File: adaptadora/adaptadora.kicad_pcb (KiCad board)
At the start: 2 copper layers, 200 x 100 mm, 107 parts, among them J1 Conn_Coaxial, J10 Conn_Coaxial, J11 Conn_Coaxial, J12 Conn_Coaxial, J13 Conn_Coaxial, J14 Conn_Coaxial, J15 Conn_Coaxial, J16 Conn_Coaxial, J17 Conn_Coaxial, J18 Conn_Coaxial, J19 Conn_Coaxial, J2 Conn_Coaxial, J20 Conn_Coaxial, J22 Conn_Coaxial, J3 Conn_Coaxial, J4 Conn_Coaxial, J5 Conn_02x20_Odd_Even, J6 Conn_01x02, J7 Conn_02x20_Odd_Even, J8 Conn_01x04, J9 Conn_01x02, U11 LM361MX_NOPB, U12 LM361MX_NOPB, U13 LM361MX_NOPB, U14 LM361MX_NOPB, U21 TLV2772IDR, U22 TLV2772IDR, U23 TLV2772IDR, U25 TLV2772IDR, U31 SN74LVC2T45DCUR, U32 SN74LVC2T45DCUR

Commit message: se ordenan campos de integrados
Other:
- board text added: "Grilla para diseño del PCB: 50 mils Grilla para el trazado de bordes de PCB: 39,37 mils (1 mm)"
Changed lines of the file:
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@@
   (general
     (thickness 1.6)
-    (drawings 31)
+    (drawings 32)
     (tracks 0)
     (zones 0)
@@
     (46 B.CrtYd user)
     (47 F.CrtYd user)
-    (48 B.Fab user hide)
-    (49 F.Fab user hide)
+    (48 B.Fab user)
+    (49 F.Fab user)
   )
   (setup
@@
     )
   )
+  (gr_text "Grilla para diseño del PCB: 50 mils\nGrilla para el trazado de bordes de PCB: 39,37 mils (1 mm)" (at 101 157) (layer Cmts.User)
+    (effects (font (size 1 1) (thickness 0.15)))
+  )
   (gr_text +3.3V (at 48.26 97.79) (layer F.SilkS)

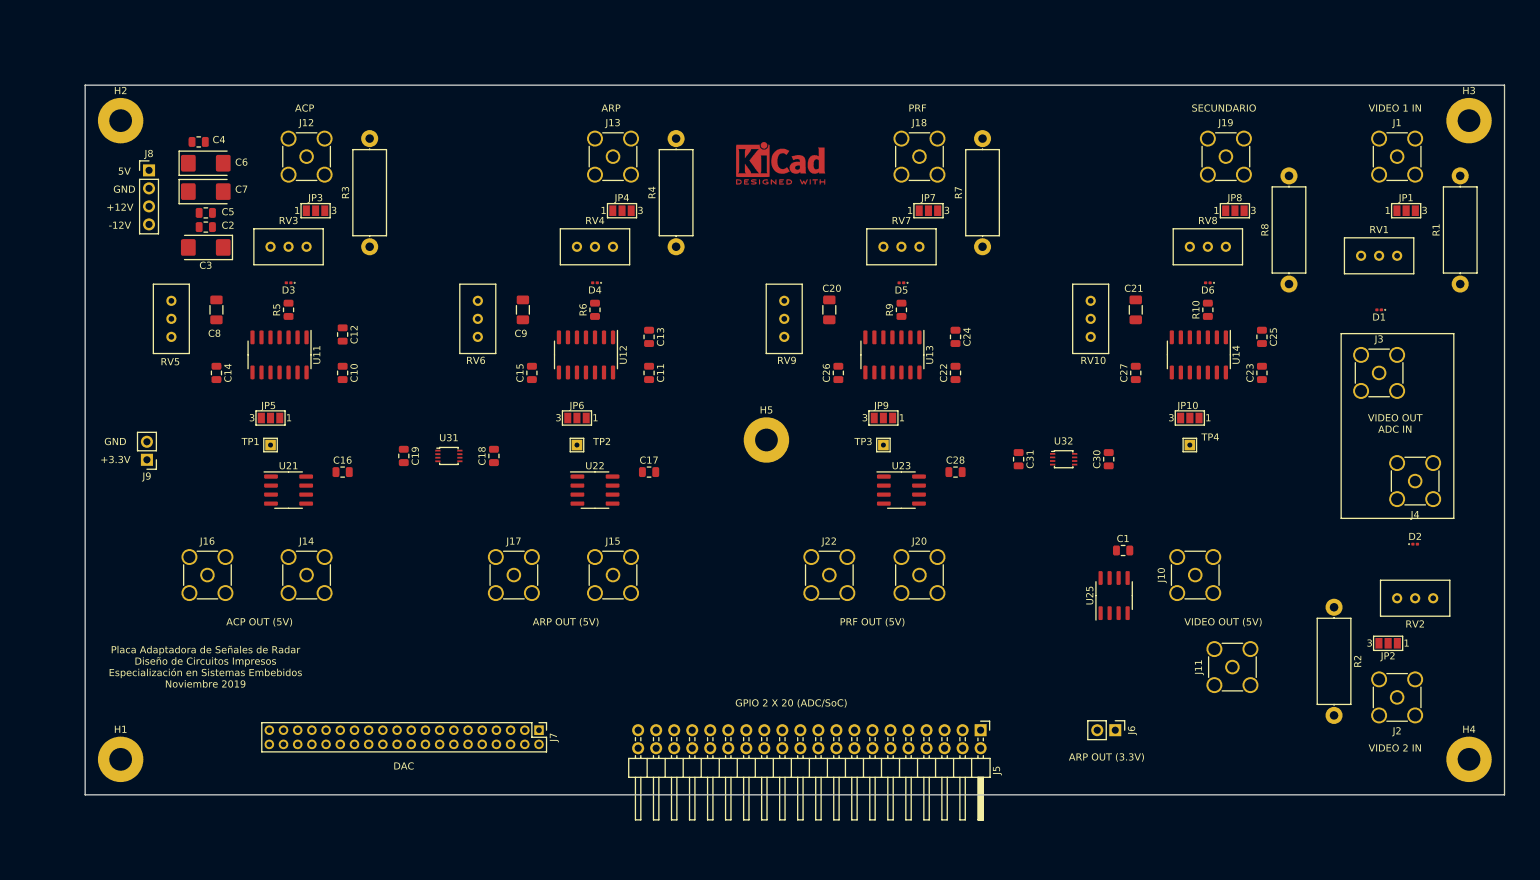
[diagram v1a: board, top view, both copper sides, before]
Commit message: se cambia footprint de componentes y el posicionamiento
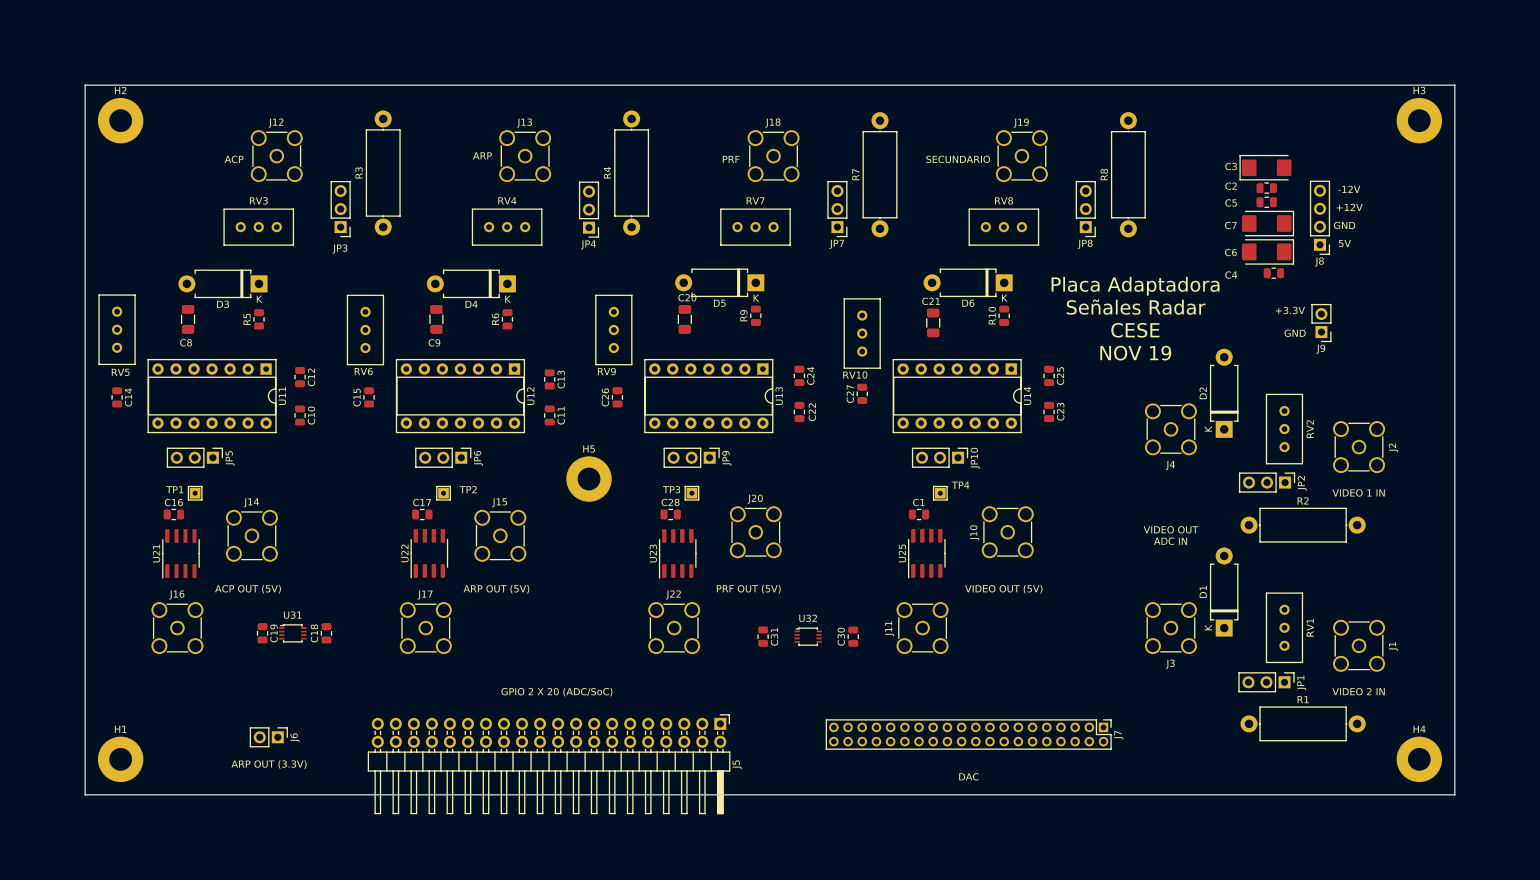
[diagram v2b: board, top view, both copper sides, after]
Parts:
- removed REF**: KiCad-Logo2_5mm_Copper, Symbol:KiCad-Logo2_5mm_Copper
- C1, C10, C11, C12, C13, C14, C15, C16, C17, C18, C19, C2, C22, C23, C24, C25, C26, C27, C28, C30, C31, C4, C5: value 0.1uF-50V -> 0_1uF-50V
- C3, C6, C7: value 2.2uF-35V -> 2_2uF-35V
- D1, D2, D3, D4, D5, D6: footprint Diode_SMD:D_0201_0603Metric -> Diode_THT:D_DO-15_P10.16mm_Horizontal
- JP1, JP10, JP2, JP3, JP4, JP5, JP6, JP7, JP8, JP9: footprint Jumper:SolderJumper-3_P1.3mm_Open_Pad1.0x1.5mm_NumberLabels -> Connector_PinHeader_2.54mm:PinHeader_1x03_P2.54mm_Vertical
- U11, U12, U13, U14: footprint Package_SO:SOIC-14_3.9x8.7mm_P1.27mm -> Package_DIP:DIP-14_W7.62mm_Socket
- moved J9 166.5 mm to (218.2, 79.8)
- moved J8 165.3 mm to (218.0, 67.5), turned to 180 degrees
- moved C4 152.6 mm to (211.5, 71.5), turned to 180 degrees
- moved C6 150.0 mm to (210.5, 68.5), turned to 180 degrees
- moved C3 149.9 mm to (210.5, 56.6), turned to 0 degrees
- moved C2 149.6 mm to (210.5, 59.5)
- moved C7 149.6 mm to (210.5, 64.5), turned to 180 degrees
- moved C5 149.5 mm to (210.5, 61.5), turned to 180 degrees
- moved J6 118.0 mm to (71.2, 136.9)
- moved J7 79.6 mm to (187.5, 135.5)
- moved J1 69.1 mm to (223.5, 124.0), turned to 270 degrees
- moved R1 68.7 mm to (208.0, 135.0), turned to 0 degrees
- moved JP1 68.6 mm to (213.0, 129.1), turned to 270 degrees
- moved RV1 57.2 mm to (213.0, 124.0), turned to 270 degrees
- moved D1 49.9 mm to (204.5, 121.5), turned to 90 degrees
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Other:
- board size 200 x 100 mm -> 193 x 100 mm
- board text added: "Grilla para diseño del PCB: 39,37 mils (1 mm) Grilla para el trazado de bordes de PCB: 39,37 mils (1 mm)"
- board text added: "Placa Adaptadora Señales Radar CESE NOV 19"
- board text removed: "Grilla para diseño del PCB: 50 mils Grilla para el trazado de bordes de PCB: 39,37 mils (1 mm)"
- board text removed: "Placa Adaptadora de Señales de Radar Diseño de Circuitos Impresos Especialización en Sistemas Embebidos Noviembre 2019"

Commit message: agrego modelo 3d lm361 sobre el sócalo
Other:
- board text added: "DCI-CESE Diseño Argentino"
- board text added: "Placa Adaptadora Señales Radar Rev. 0 - Nov 19"
- board text removed: "Placa Adaptadora Señales Radar CESE NOV 19"
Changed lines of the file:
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@@
   (general
     (thickness 1.6)
-    (drawings 28)
+    (drawings 29)
     (tracks 0)
     (zones 0)
@@
   )
   (layers
-    (0 F.Cu signal hide)
-    (31 B.Cu signal hide)
-    (32 B.Adhes user hide)
-    (33 F.Adhes user hide)
-    (34 B.Paste user hide)
-    (35 F.Paste user hide)
-    (36 B.SilkS user hide)
-    (37 F.SilkS user hide)
-    (38 B.Mask user hide)
-    (39 F.Mask user hide)
-    (40 Dwgs.User user hide)
-    (41 Cmts.User user hide)
-    (42 Eco1.User user hide)
-    (43 Eco2.User user hide)
-    (44 Edge.Cuts user hide)
-    (45 Margin user hide)
-    (46 B.CrtYd user hide)
-    (47 F.CrtYd user hide)
-    (48 B.Fab user hide)
-    (49 F.Fab user hide)
+    (0 F.Cu signal)
+    (31 B.Cu signal)
+    (32 B.Adhes user)
+    (33 F.Adhes user)
+    (34 B.Paste user)
+    (35 F.Paste user)
+    (36 B.SilkS user)
+    (37 F.SilkS user)
+    (38 B.Mask user)
+    (39 F.Mask user)
+    (40 Dwgs.User user)
+    (41 Cmts.User user)
+    (42 Eco1.User user)
+    (43 Eco2.User user)
+    (44 Edge.Cuts user)
+    (45 Margin user)
+    (46 B.CrtYd user)
+    (47 F.CrtYd user)
+    (48 B.Fab user)
+    (49 F.Fab user)
   )
   (setup
@@
       (rotate (xyz 0 0 0))
     )
+    (model ${KISYS3DMOD}/Package_DIP.3dshapes/DIP-14_W7.62mm.wrl
+      (offset (xyz 0 0 4))
+      (scale (xyz 1 1 1))
+      (rotate (xyz 0 0 0))
+    )
   )
   (module Package_DIP:DIP-14_W7.62mm_Socket (layer F.Cu)
@@
       (rotate (xyz 0 0 0))
     )
+    (model ${KISYS3DMOD}/Package_DIP.3dshapes/DIP-14_W7.62mm.wrl
+      (offset (xyz 0 0 4))
+      (scale (xyz 1 1 1))
+      (rotate (xyz 0 0 0))
+    )
   )
   (module Package_DIP:DIP-14_W7.62mm_Socket (layer F.Cu)
@@
       (rotate (xyz 0 0 0))
     )
+    (model ${KISYS3DMOD}/Package_DIP.3dshapes/DIP-14_W7.62mm.wrl
+      (offset (xyz 0 0 4))
+      (scale (xyz 1 1 1))
+      (rotate (xyz 0 0 0))
+    )
   )
   (module Package_DIP:DIP-14_W7.62mm_Socket (layer F.Cu)
@@
       (rotate (xyz 0 0 0))
     )
+    (model ${KISYS3DMOD}/Package_DIP.3dshapes/DIP-14_W7.62mm.wrl
+      (offset (xyz 0 0 4))
+      (scale (xyz 1 1 1))
+      (rotate (xyz 0 0 0))
+    )
   )
   (module Diode_THT:D_DO-15_P10.16mm_Horizontal (layer F.Cu)
@@
     (descr "Through hole straight pin header, 1x04, 2.54mm pitch, single row")
     (tags "Through hole pin header THT 1x04 2.54mm single row")
-    (fp_text reference J8 (at 0 -2.33) (layer F.SilkS)
+    (fp_text reference J8 (at 0 -3) (layer F.SilkS)
       (effects (font (size 1 1) (thickness 0.15)))
     )
@@
     (descr "Through hole straight pin header, 1x02, 2.54mm pitch, single row")
     (tags "Through hole pin header THT 1x02 2.54mm single row")
-    (fp_text reference J9 (at 0 -2.33) (layer F.SilkS)
+    (fp_text reference J9 (at 0 -2.71) (layer F.SilkS)
       (effects (font (size 1 1) (thickness 0.15)))
     )
@@
     (tags "test point THT pad rectangle square")
     (attr virtual)
-    (fp_text reference TP1 (at -2.81 -0.46) (layer F.SilkS)
+    (fp_text reference TP1 (at 3 -0.5) (layer F.SilkS)
       (effects (font (size 1 1) (thickness 0.15)))
     )
@@
     )
   )
+  (gr_text "DCI-CESE\nDiseño\nArgentino\n" (at 53.5 62) (layer F.SilkS)
+    (effects (font (size 1.5 1.5) (thickness 0.2)))
+  )
   (dimension 193 (width 0.15) (layer Dwgs.User)
     (gr_text "193,000 mm" (at 140.5 34.7) (layer Dwgs.User)
@@
     (effects (font (size 1 1) (thickness 0.15)))
   )
-  (gr_text +3.3V (at 213.76 76.79) (layer F.SilkS)
+  (gr_text +3.3V (at 222.5 76.79) (layer F.SilkS)
     (effects (font (size 1 1) (thickness 0.15)))
   )
-  (gr_text GND (at 214.5 80) (layer F.SilkS)
+  (gr_text GND (at 222 80) (layer F.SilkS)
     (effects (font (size 1 1) (thickness 0.15)))
   )
@@
     (effects (font (size 1 1) (thickness 0.15)))
   )
-  (gr_text "Placa Adaptadora \nSeñales Radar\nCESE\nNOV 19" (at 192 78) (layer F.SilkS)
-    (effects (font (size 2 2) (thickness 0.15)))
+  (gr_text "Placa Adaptadora \nSeñales Radar\nRev. 0 - Nov 19" (at 195 76.5) (layer F.SilkS)
+    (effects (font (size 1.5 1.5) (thickness 0.2)))
   )
   (dimension 100 (width 0.15) (layer Dwgs.User)

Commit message: ruteo en proceso
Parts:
- R10: value 100 - 1/8W - 5% -> 100-1/8W-5%
- moved J7 38.5 mm to (149.0, 137.0), turned to 90 degrees
- moved J20 17.9 mm to (120.8, 110.5)
- moved C19 15.4 mm to (84.0, 125.8), turned to 180 degrees
- moved U31 14.6 mm to (87.8, 124.0), turned to 90 degrees
- moved C16 13.2 mm to (69.8, 105.5)
- moved C17 13.2 mm to (104.8, 105.5)
- moved J16 13.2 mm to (70.2, 121.5)
- moved J17 13.2 mm to (105.2, 121.5)
- moved U21 13.2 mm to (70.8, 111.0)
- moved U22 13.2 mm to (105.8, 111.0)
- moved C14 12.4 mm to (57.0, 80.0)
- moved C15 12.0 mm to (92.0, 80.0), turned to 270 degrees
- moved C26 12.0 mm to (127.0, 80.0), turned to 270 degrees
- moved C27 12.0 mm to (162.0, 80.0), turned to 270 degrees
- moved J14 9.71 mm to (58.0, 110.5)
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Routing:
- net GND: track 0.00 -> 362.7 mm
- net +5V: track 0.00 -> 347.8 mm, vias 0 -> 2
- net -12V: track 0.00 -> 208.2 mm
- net +12V: track 0.00 -> 192.9 mm
- net Net-(C9-Pad1): track 0.00 -> 20.3 mm
- net Net-(C20-Pad1): track 0.00 -> 20.3 mm
- net Net-(C8-Pad1): track 0.00 -> 20.3 mm
- net Net-(J13-Pad1): track 0.00 -> 19.0 mm
- net Net-(J19-Pad1): track 0.00 -> 19.0 mm
- net Net-(J18-Pad1): track 0.00 -> 19.0 mm
- net Net-(J12-Pad1): track 0.00 -> 19.0 mm
- net Net-(C21-Pad1): track 0.00 -> 17.8 mm
- net Net-(D2-Pad1): track 0.00 -> 16.0 mm
- net Net-(D1-Pad1): track 0.00 -> 16.0 mm
- net Net-(J1-Pad1): track 0.00 -> 15.6 mm
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
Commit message: ruteo en proceso
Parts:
- moved J20 24.3 mm to (141.0, 124.0)
- moved J14 18.7 mm to (71.0, 124.0)
- moved J15 17.5 mm to (106.0, 124.0)
- moved J10 16.1 mm to (176.0, 124.0)
- moved C18 15.7 mm to (78.0, 108.0)
- moved C19 15.7 mm to (78.0, 111.2)
- moved U31 15.7 mm to (81.8, 109.5)
- moved C30 13.4 mm to (144.2, 108.0)
- moved C31 13.4 mm to (144.2, 111.0)
- moved U32 13.2 mm to (149.0, 109.6)
- moved J16 11.5 mm to (59.0, 124.0)
- moved J17 11.5 mm to (94.0, 124.0)
- moved U21 11.3 mm to (59.5, 109.5), turned to 0 degrees
- moved U22 11.3 mm to (94.5, 109.5), turned to 0 degrees
- moved C28 9.71 mm to (136.0, 107.5)
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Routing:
- net GND: track 362.7 -> 273.4 mm
- net /Señales de ACP y ARP/ACP: track 5.02 -> 43.3 mm
- net /Señales de ACP y ARP/ARP: track 5.02 -> 33.8 mm
- net Net-(J14-Pad1): track 0.00 -> 19.9 mm
- net Net-(J20-Pad1): track 1.11 -> 20.1 mm
- net Net-(J15-Pad1): track 1.14 -> 20.1 mm
- net /Señales de Video Secundario y PRF/VIDEO_COMP: track 5.02 -> 23.0 mm
- net /Señales de Video Secundario y PRF/PRF: track 5.02 -> 18.6 mm
- net Net-(J10-Pad1): track 13.8 -> 25.9 mm
- net Net-(J22-Pad1): track 9.35 -> 19.7 mm
- net Net-(J17-Pad1): track 9.38 -> 19.7 mm
- net Net-(J16-Pad1): track 9.35 -> 19.3 mm
- net +3V3: track 0.00 -> 5.25 mm
- net Net-(J11-Pad1): track 9.34 -> 13.2 mm
- net +5V: track 347.8 -> 349.2 mm

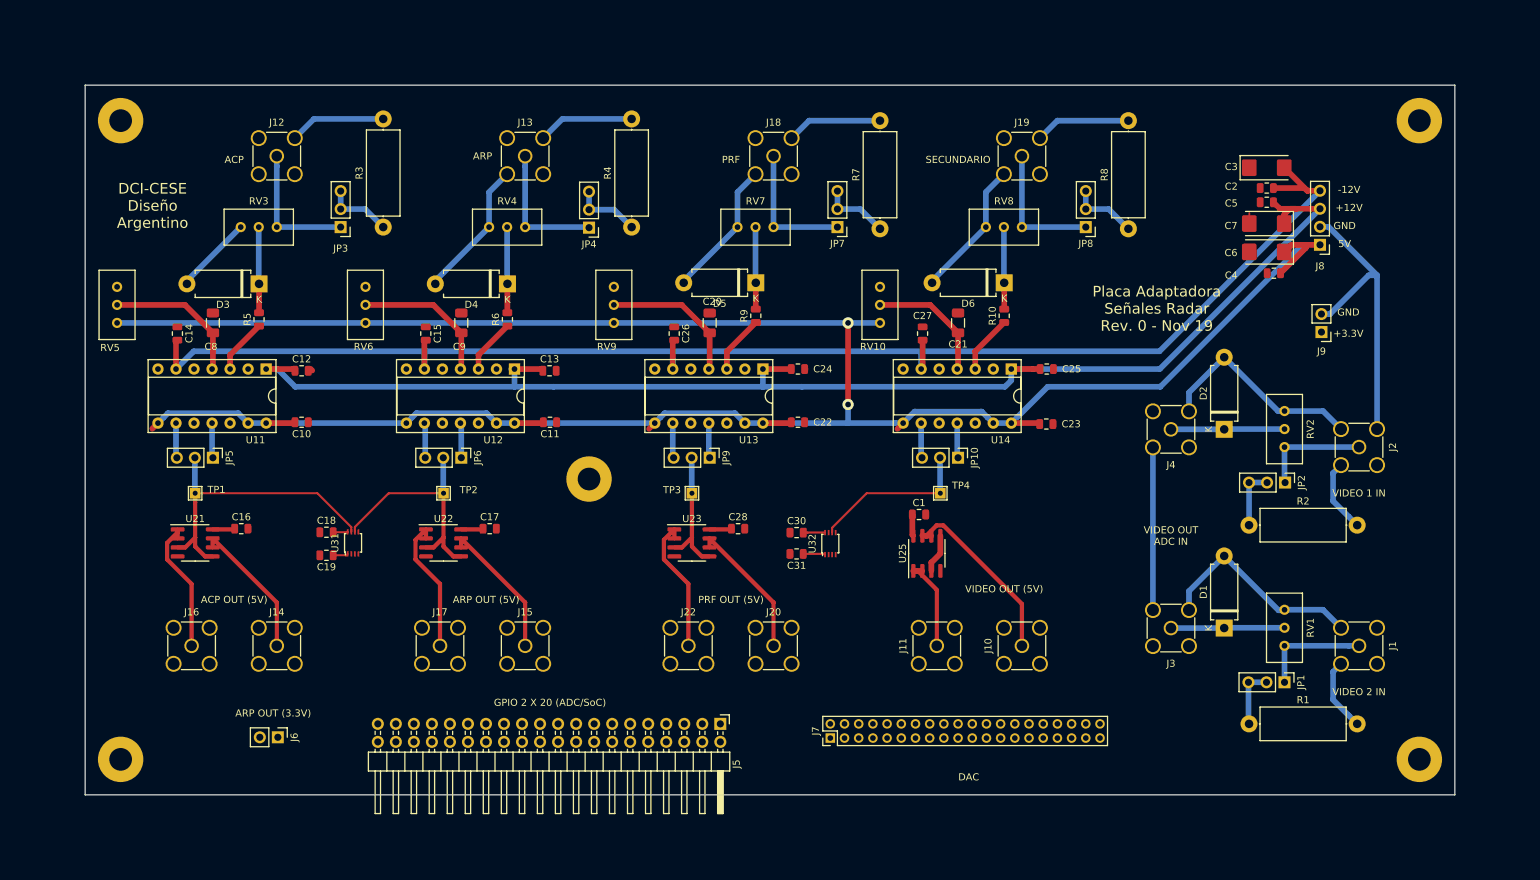
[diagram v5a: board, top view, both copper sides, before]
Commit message: ultimo commit antes de quitar dac del esq
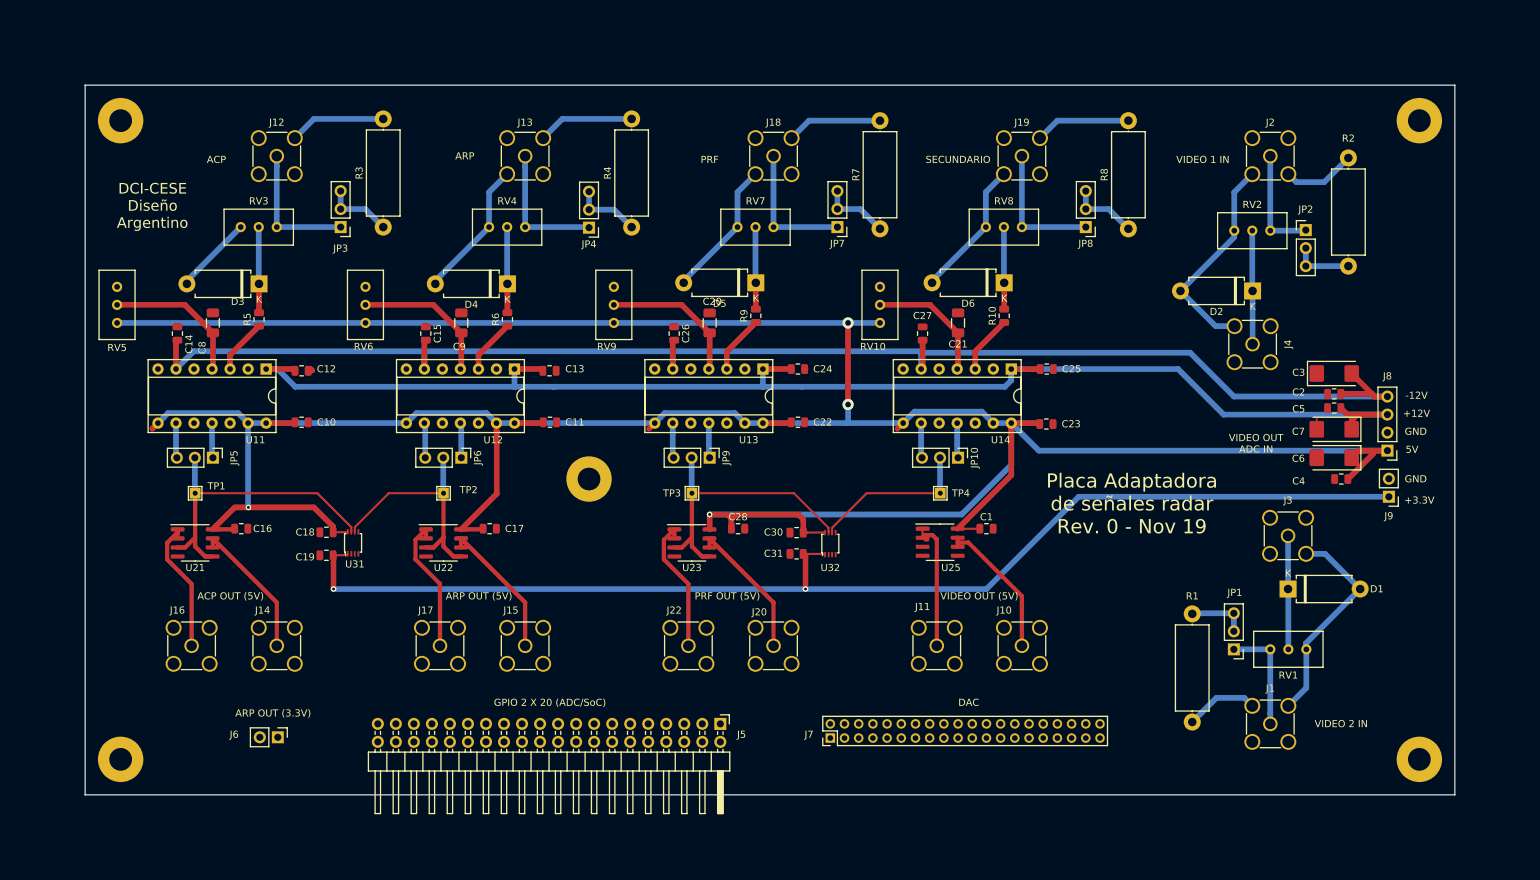
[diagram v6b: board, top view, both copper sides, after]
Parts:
- R5, R6, R9: value 100 - 1/8W - 5% -> 100-1/8W-5%
- moved J2 42.9 mm to (211.0, 55.0), turned to 0 degrees
- moved R2 39.1 mm to (222.0, 70.5), turned to 90 degrees
- moved JP2 35.7 mm to (216.0, 65.4), turned to 0 degrees
- moved RV2 30.6 mm to (211.0, 65.5), turned to 0 degrees
- moved C2 30.5 mm to (220.0, 88.5)
- moved C4 30.5 mm to (221.0, 100.5)
- moved C5 30.5 mm to (220.0, 90.5)
- moved C6 30.5 mm to (220.0, 97.5)
- moved C7 30.5 mm to (220.0, 93.5)
- moved J8 30.5 mm to (227.5, 96.5)
- moved C3 30.5 mm to (220.0, 85.6)
- moved J9 25.1 mm to (227.7, 103.0)
- moved J3 21.0 mm to (213.5, 108.5), turned to 180 degrees
- moved D2 19.9 mm to (208.5, 74.0), turned to 180 degrees
- moved R1 17.4 mm to (200.0, 119.5), turned to 270 degrees
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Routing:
- net +3V3: track 5.25 -> 169.2 mm, vias 0 -> 2
- net +5V: track 349.2 -> 484.8 mm, vias 2 -> 4
- net GND: track 273.4 -> 207.9 mm
- net /Señales de Video Secundario y PRF/PRF: track 18.6 -> 40.6 mm
- net Net-(J11-Pad1): track 13.2 -> 19.6 mm
- net +12V: track 192.9 -> 198.7 mm
- net /VIDEO_DIGITAL: track 5.48 -> 0.00 mm
- net Net-(J10-Pad1): track 25.9 -> 20.4 mm
- net -12V: track 208.2 -> 211.1 mm
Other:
- board text added: "Placa Adaptadora de señales radar Rev. 0 - Nov 19"
- board text removed: "Placa Adaptadora Señales Radar Rev. 0 - Nov 19"
